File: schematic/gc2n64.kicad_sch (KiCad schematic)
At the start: 12 parts, among them J1 Conn_01x03, J2 Conn_01x03, U1 ATtiny85-20P

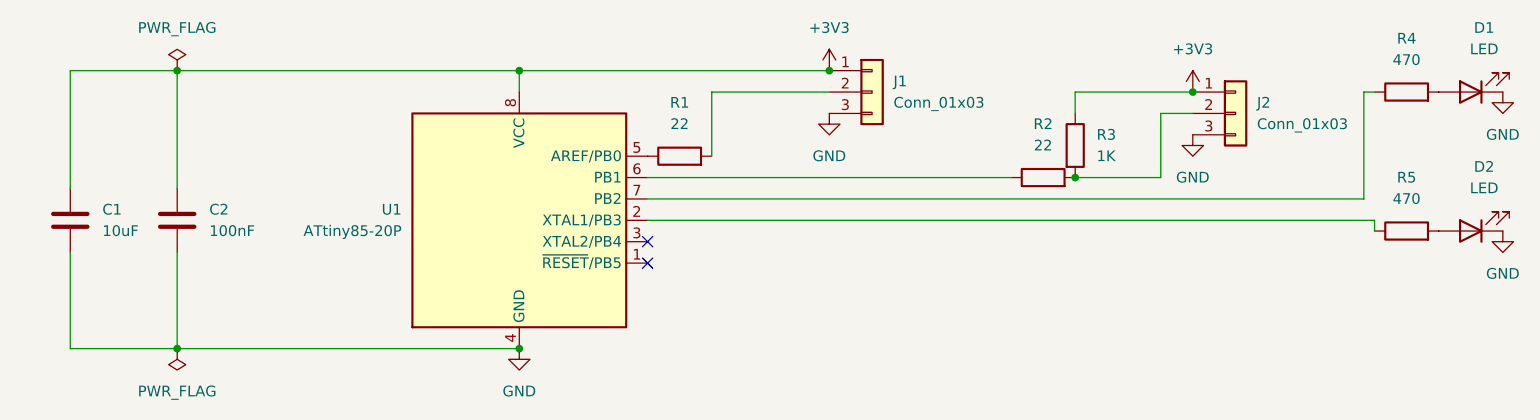
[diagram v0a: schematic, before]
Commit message: feat(design): revision 2
Refactored the design to work with either attiny9 or attiny25, using a
basic hardware abstraction layer. So that the PCB can have a tagconnect
footprint rather than excessive through holes and plugging and
unplugging of attiny85 into a socket.
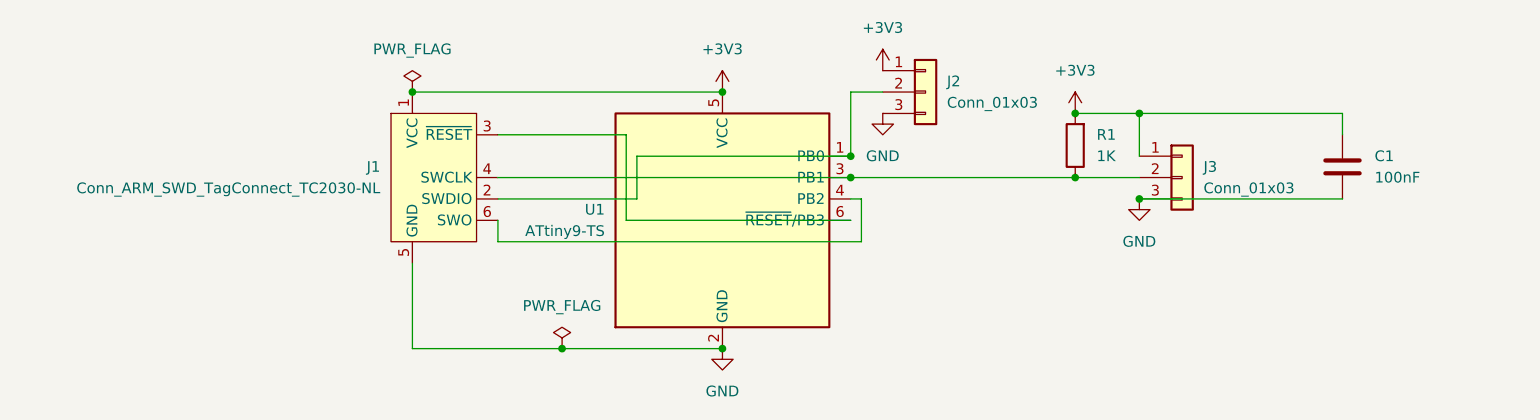
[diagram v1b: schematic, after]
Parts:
- removed C2: 100nF, Capacitor_SMD:C_0805_2012Metric, symbol Device:C
- removed D1, D2: LED, LED_SMD:LED_0805_2012Metric, symbol Device:LED
- removed J1: Conn_01x03, Connector_PinHeader_2.54mm:PinHeader_1x03_P2.54mm_Vertical, symbol Connector_Generic:Conn_01x03
- removed R2: 22, Resistor_SMD:R_0805_2012Metric, symbol Device:R
- removed R3: 1K, Resistor_SMD:R_0805_2012Metric, symbol Device:R
- removed R4, R5: 470, Resistor_SMD:R_0805_2012Metric, symbol Device:R
- removed U1: ATtiny85-20P, Package_DIP:DIP-8_W7.62mm, symbol MCU_Microchip_ATtiny:ATtiny85-20P
- added J1: Conn_ARM_SWD_TagConnect_TC2030-NL, Connector:Tag-Connect_TC2030-IDC-NL_2x03_P1.27mm_Vertical, symbol Connector:Conn_ARM_SWD_TagConnect_TC2030-NL
- added J3: Conn_01x03, Connector_Wire:SolderWire-0.1sqmm_1x03_P3.6mm_D0.4mm_OD1mm_Relief2x, symbol Connector_Generic:Conn_01x03
- added U1: ATtiny9-TS, Package_TO_SOT_SMD:SOT-23-6, symbol MCU_Microchip_ATtiny:ATtiny9-TS
- C1: value 10uF -> 100nF; footprint Capacitor_SMD:C_0805_2012Metric -> Capacitor_SMD:C_0402_1005Metric
- J2: footprint Connector_PinHeader_2.54mm:PinHeader_1x03_P2.54mm_Vertical -> Connector_Wire:SolderWire-0.1sqmm_1x03_P3.6mm_D0.4mm_OD1mm_Relief2x
- R1: value 22 -> 1K; footprint Resistor_SMD:R_0805_2012Metric -> Resistor_SMD:R_0402_1005Metric
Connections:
- net +3V3: now also R1.2, J1.1 (VCC), J3.1 (Pin_1), U1.5 (VCC)
- net GND: now also J1.5 (GND), J3.3 (Pin_3), U1.2 (GND)
- net at J2.2 (Pin_2): now also J1.2 (SWDIO), U1.1 (PB0)
- net at R1.1: now also J1.4 (SWCLK), J3.2 (Pin_2), U1.3 (PB1)
- new net: J1.3 (~{RESET}), U1.6 (~{RESET}/PB3)
- new net: J1.6 (SWO), U1.4 (PB2)
- no-connect marks 2 -> 0
